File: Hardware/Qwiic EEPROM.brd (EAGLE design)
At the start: 25.4 x 25.4 mm, 56 parts, among them J3 PTH, U1 RM24C512C

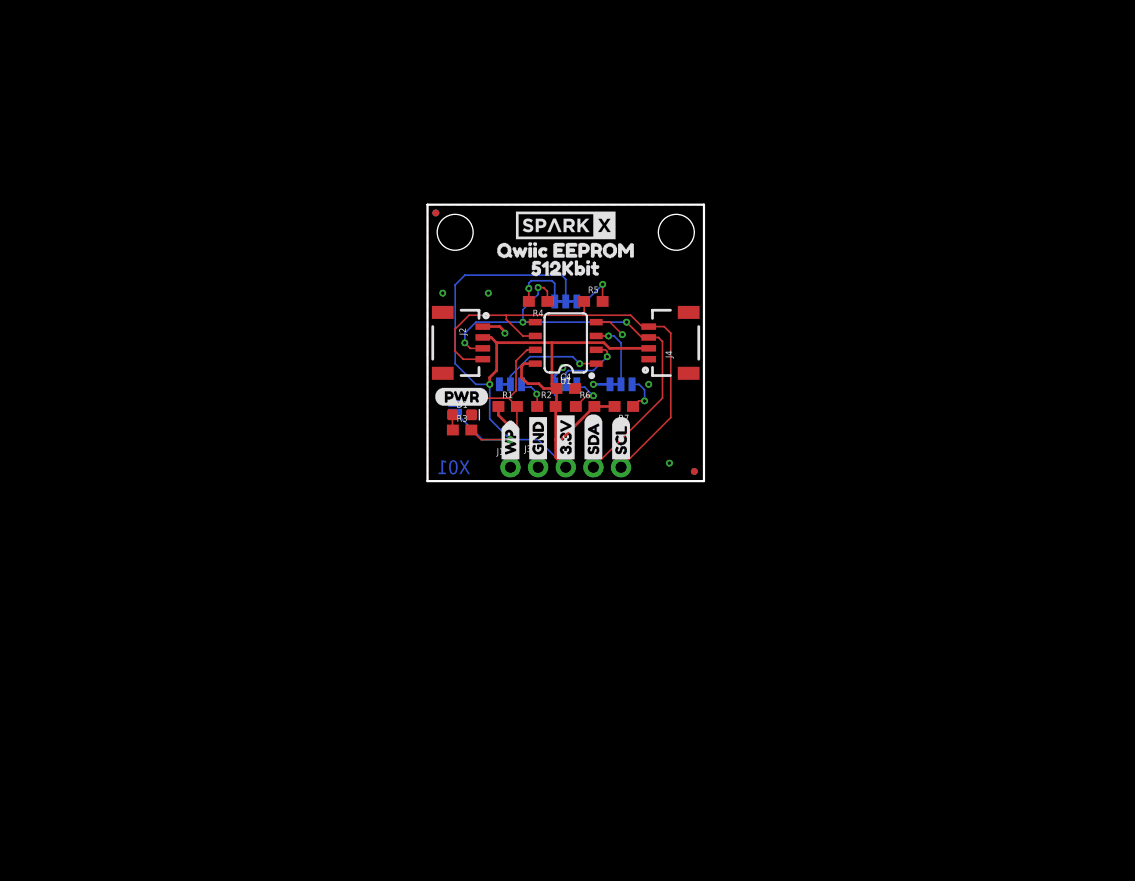
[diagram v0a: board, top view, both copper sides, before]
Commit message: Add datasheet, make sure all parts are from SF libraries
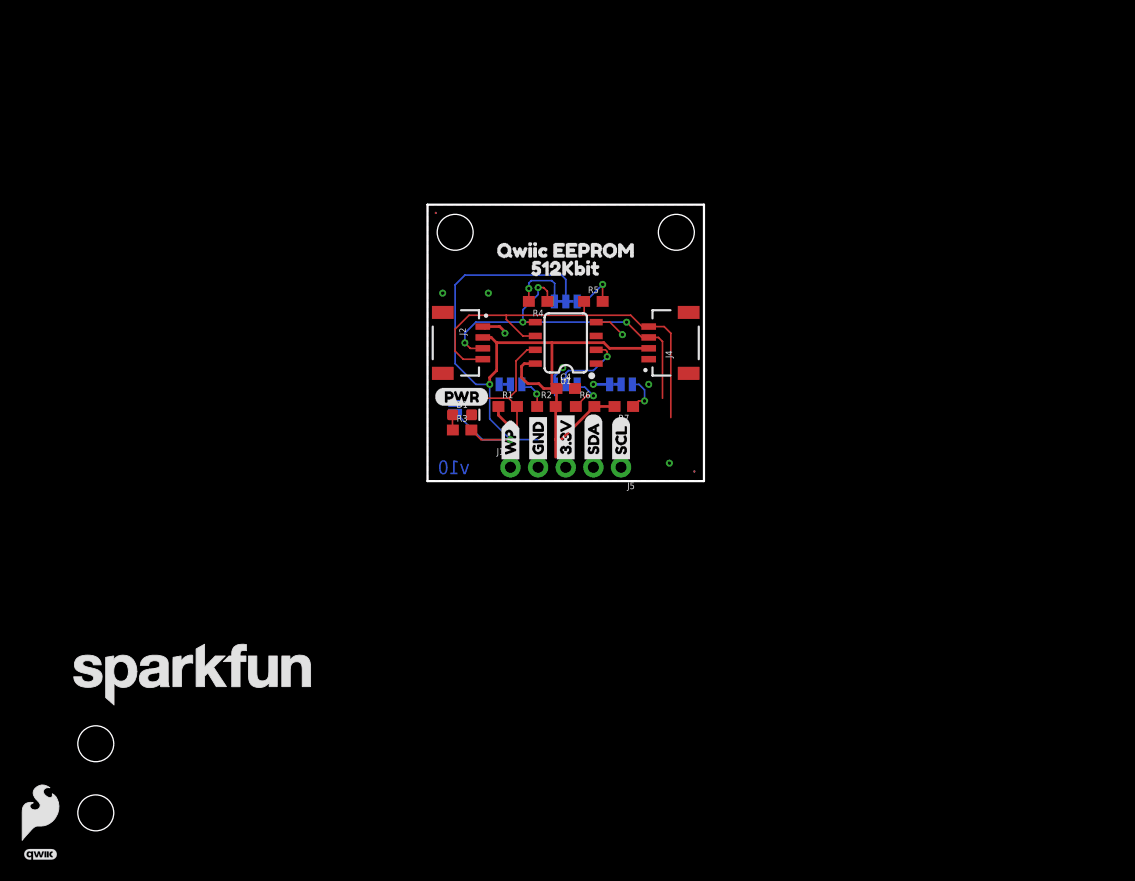
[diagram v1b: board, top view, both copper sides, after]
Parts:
- removed J3: PTH, SparkX:1X04_NO_SILK
- removed U$1, U$2: SPARKX-LOGO4, SparkX:SPARKX-MEDIUM
- added J5: (no value), SparkFun-Connectors:1X04_NO_SILK
- added JP7, JP8: STAND-OFF, SparkFun-Hardware:STAND-OFF
- added LOGO2: SFE_LOGO_NAME.2_INCH, SparkFun-Aesthetics:SFE_LOGO_NAME_.2
- added LOGO3: SFE_LOGO_FLAME.2_INCH, SparkFun-Aesthetics:SFE_LOGO_FLAME_.2
- added LOGO4: QWIIC_LOGO_3MM, SparkFun-Aesthetics:QWIIC_3MM
- E0, E1, E2: value (none) -> JUMPER-SMT_3_1-NC_TRACE_SILK
- I2C: value (none) -> JUMPER-SMT_3_2-NC_TRACE_SILK
- J2, J4: value (none) -> QWIIC_RA; device SparkFun-Connectors:1X04_1MM_RA -> SparkFun-Connectors:JST04_1MM_RA
- JP1, JP2, JP5, JP6: value FIDUCIALUFIDUCIAL -> FIDUCIAL0.2MM; device SparkFun:MICRO-FIDUCIAL -> SparkFun-Aesthetics:FIDUCIAL-0.2MM
- JP3, JP4: device SparkFun:STAND-OFF -> SparkFun-Hardware:STAND-OFF
- R4, R5: value 2.2k -> 4.7k
- WP: value (none) -> JUMPER-SMT_2_NO_SILK
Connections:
- net 3.3V: now also J5.3; no longer J3.2
- net GND: now also J5.4; no longer J3.1
- net SCL: now also J5.1; no longer J3.4
- net SDA: now also J5.2; no longer J3.3
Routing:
- net N$6: track 9.81 -> 0.00 mm, vias 1 -> 0
- net SDA: track 43.1 -> 34.1 mm
- net SCL: track 45.1 -> 38.6 mm
- net N$4: track 6.35 -> 0.00 mm, vias 1 -> 0
- net 3.3V: track 93.4 -> 87.3 mm
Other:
- board text added: "Revised by: Priyanka Makin"
- board text added: "v10"
- board text removed: "X01"

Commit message: Hardware updates
Schematic symbols from current SF libs
Added mounting holes
re-routing
Update 3.3V rail width
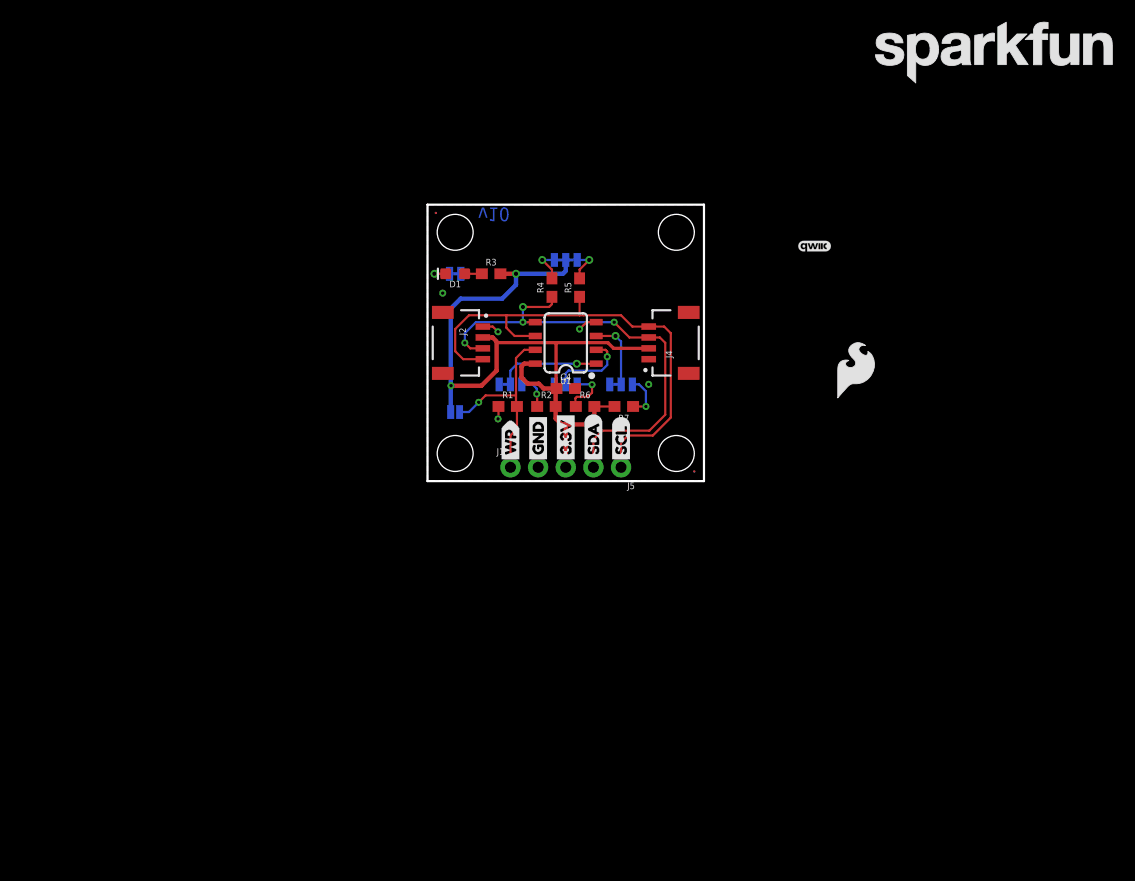
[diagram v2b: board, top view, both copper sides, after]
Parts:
- removed U$10: (no value), Labels-0_04:(PWR)
- removed U$14, U$17: (no value), buzzard_labels:512KBIT7
- removed U$15, U$16: (no value), buzzard_labels:QWIIC_EEPROM2
- removed U$29: (no value), Labels:QWIIC-LOGO-MEDIUM
- added POWER: JUMPER-SMT_2_NC_TRACE_SILK, SparkFun-Jumpers:SMT-JUMPER_2_NC_TRACE_SILK
- moved LOGO2 93.2 mm to (52.1, 39.4)
- moved LOGO4 90.4 mm to (35.6, 21.6)
- moved LOGO3 85.2 mm to (39.4, 10.2)
- moved JP8 62.7 mm to (22.9, 2.54)
- moved JP7 42.4 mm to (2.54, 2.54)
- moved LOGO1 28.5 mm to (29.2, 14.0)
- moved R3 14.6 mm to (5.84, 19.1)
- moved D1 13.0 mm to (2.54, 19.1), turned to 180 degrees
- moved I2C 3.81 mm to (12.7, 20.3)
- moved R4 1.80 mm to (11.4, 17.8), turned to 90 degrees
- moved R5 1.80 mm to (14.0, 17.8), turned to 90 degrees
- moved WP 0.38 mm to (2.54, 6.35), turned to 0 degrees
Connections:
- new net N$10: D1.C, POWER.2
- net GND: now also POWER.1; no longer D1.C
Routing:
- net 3.3V: track 87.3 -> 71.6 mm
- net SDA: track 34.1 -> 45.0 mm
- net N$6: track 0.00 -> 9.42 mm, vias 0 -> 1
- net SCL: track 38.6 -> 47.3 mm
- net GND: track 12.1 -> 4.55 mm, vias 9 -> 5
- net N$4: track 0.00 -> 6.43 mm, vias 0 -> 1
- net N$2: track 5.91 -> 3.18 mm
- net N$10: track 0.00 -> 2.41 mm, vias 0 -> 1
- net N$1: track 4.56 -> 3.18 mm

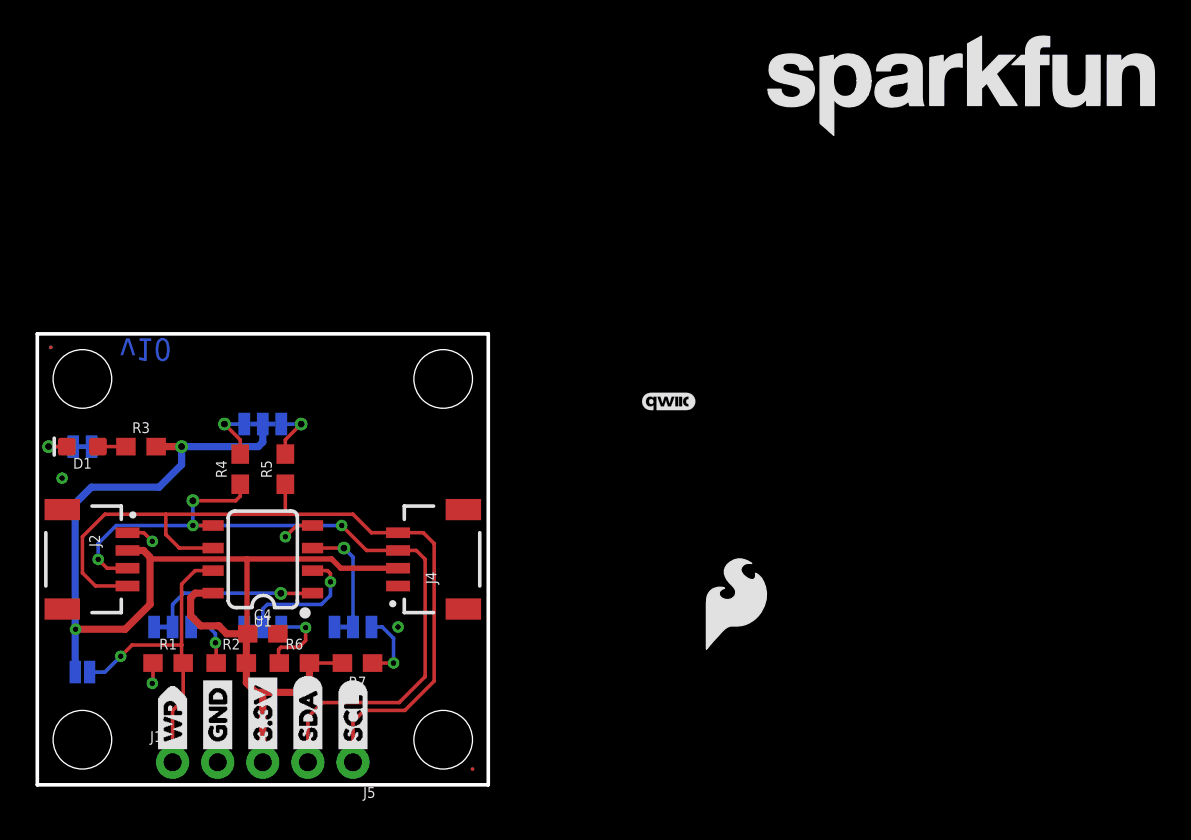
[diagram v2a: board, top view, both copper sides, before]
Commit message: Vectorize labels
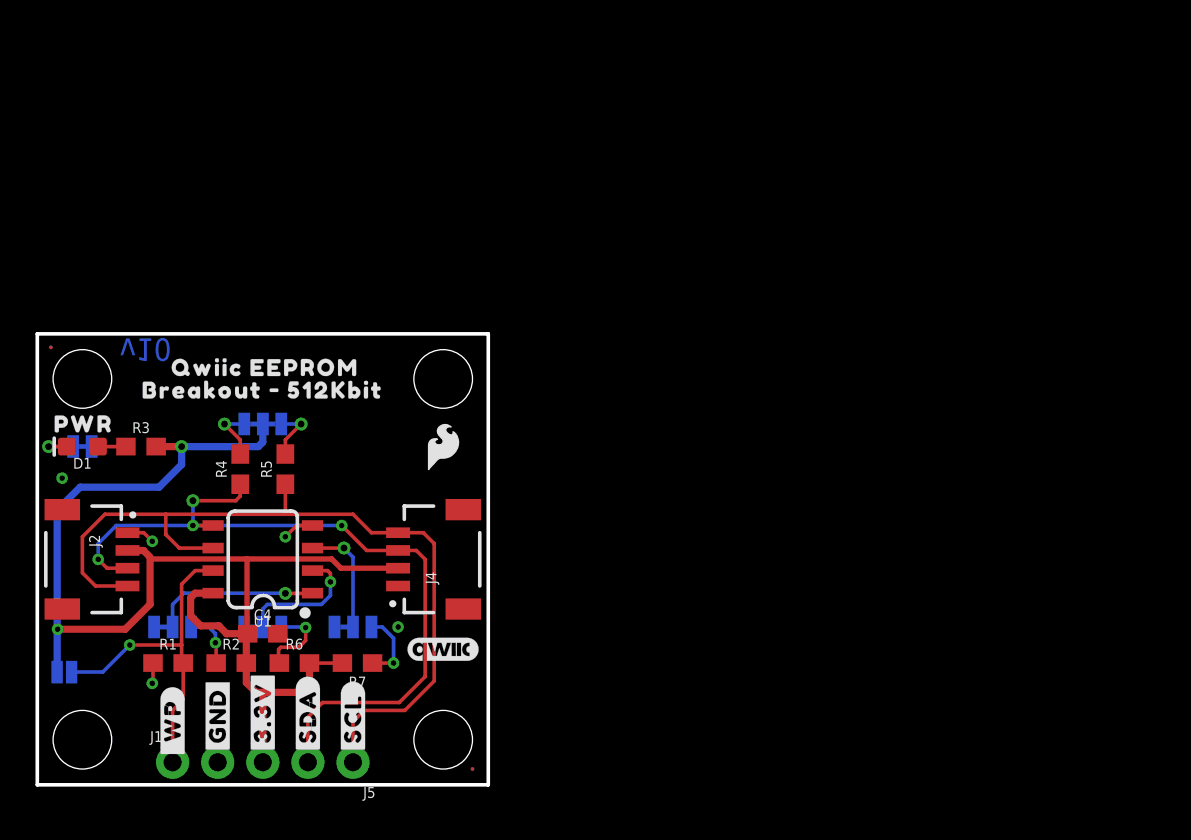
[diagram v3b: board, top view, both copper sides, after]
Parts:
- removed U$25, U$28: (no value), buzzard_labels (2):WP2
- removed U$26: (no value), Labels-0_04:SCL9
- removed U$27: (no value), Labels-0_04:SDA8
- added U$1, U$2: (no value), output:#_WP#0
- added U$10, U$14: (no value), output:#GND#0
- added U$15, U$16: (no value), output:#3#3V#0
- added U$17, U$29: (no value), output:#SDA#0
- added U$30, U$31: (no value), output:#SCL#0
- LOGO2: value SFE_LOGO_NAME.2_INCH -> SFE_LOGO_NAME.1_INCH; device SparkFun-Aesthetics:SFE_LOGO_NAME_.2 -> SparkFun-Aesthetics:SFE_LOGO_NAME_.1
- LOGO3: value SFE_LOGO_FLAME.2_INCH -> SFE_LOGO_FLAME.1_INCH; device SparkFun-Aesthetics:SFE_LOGO_FLAME_.2 -> SparkFun-Aesthetics:SFE_LOGO_FLAME_.1
- LOGO4: value QWIIC_LOGO_3MM -> QWIIC_LOGO_4MM; device SparkFun-Aesthetics:QWIIC_3MM -> SparkFun-Aesthetics:QWIIC_4MM
- U$12: device buzzard_labels (1):00 -> output:PWR0
- U$13: device buzzard_labels:E14 -> output:10
- U$18: device buzzard_labels (1):00 -> output:#PWR#0
- U$19: device buzzard_labels (1):00 -> output:QWIIC_EEPROM0
- U$20: device buzzard_labels (1):11 -> output:QWIIC_EEPROM0
- U$21: device Labels-0_04:3#3V2 -> output:10
- U$22: device Labels-0_04:GND1 -> output:10
- U$23, U$24: device buzzard_labels (1):11 -> output:BREAKOUT_#_512KBIT0
- U$3: device Labels-0_04:GND1 -> output:#WP#0
- U$4: device Labels-0_04:3#3V2 -> output:E00
- U$5: device Labels-0_04:SDA8 -> output:E10
- U$6: device Labels-0_04:SCL9 -> output:E20
- U$7: device buzzard_labels:WP6 -> output:00
- U$8: device buzzard_labels:E05 -> output:00
- U$9: device buzzard_labels:E23 -> output:00
- moved LOGO2 46.9 mm to (12.7, 14.0), flipped to the bottom
- moved U$12 22.5 mm to (0.25, 20.3), flipped to the top
- moved LOGO4 18.9 mm to (22.9, 7.62)
- moved LOGO3 18.8 mm to (22.9, 19.1)
- moved U$23 18.3 mm to (5.21, 22.2), flipped to the top
- moved U$24 18.1 mm to (20.1, 22.2)
- moved U$20 16.6 mm to (18.7, 23.5)
- moved U$19 16.6 mm to (6.86, 23.5), flipped to the top
- moved U$18 13.0 mm to (8.13, 18.9)
- moved LOGO1 9.92 mm to (22.9, 6.35)
- moved U$4 9.81 mm to (9.14, 10.7), turned to 0 degrees
- moved U$6 9.27 mm to (19.3, 10.7), turned to 0 degrees
- moved U$5 9.20 mm to (14.2, 10.7), turned to 0 degrees
- moved U$13 6.43 mm to (19.8, 6.99)
- moved U$3 6.31 mm to (6.10, 6.35), turned to 0 degrees
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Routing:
- net 3.3V: track 71.6 -> 73.4 mm
- net WP: track 18.2 -> 19.2 mm

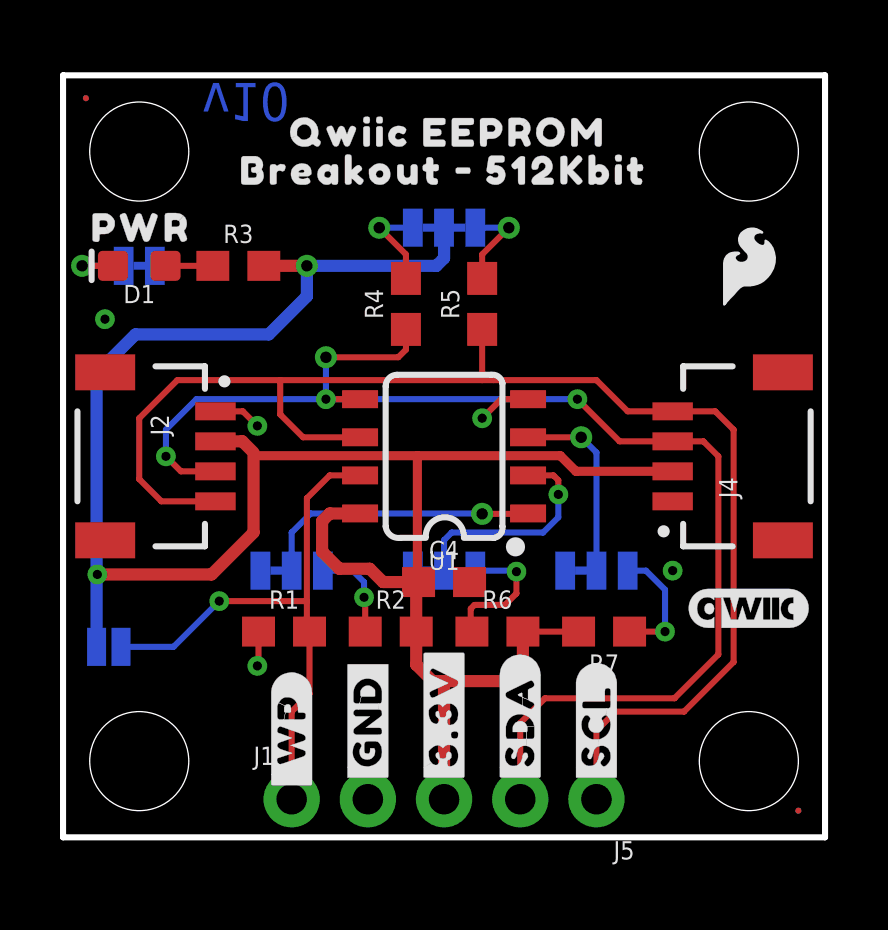
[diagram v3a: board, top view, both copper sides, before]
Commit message: Design review changes
Schematic:
* Added Vcc range for EEPROM IC
* Updated notes for power led and address jumpers
* Got rid of legacy font
* Replaced pullup/pulldown resistors R1, R2, R6, R7 to 100k

Board:
* Weird tRestrict on GND pad of EEPROM IC --> moved via around to avoid DRC errors
* Moved "PWR" label underneath the LED
* Moved "I2C" label so that it touches the silk of the jumper above it
* Re-routed 3.3V trace so that it does not run under the EEPROM IC
* Increased size of fiducials
* Made vias all the same size
* Added prod-id to the EEPROM IC
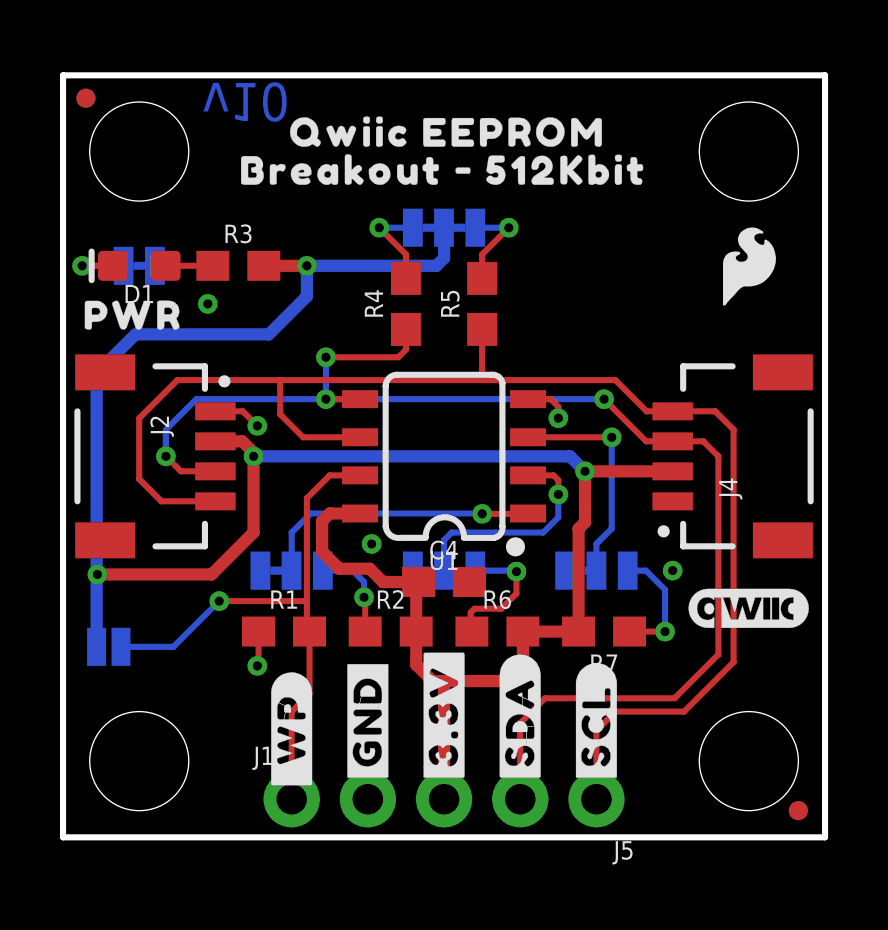
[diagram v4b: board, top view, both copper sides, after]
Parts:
- JP1, JP2, JP5, JP6: value FIDUCIAL0.2MM -> FIDUCIALUFIDUCIAL; device SparkFun-Aesthetics:FIDUCIAL-0.2MM -> SparkFun-Aesthetics:FIDUCIAL-MICRO
- R1, R2, R6, R7: value 10k -> 100k
- moved U$12 2.93 mm to (0.00, 17.4)
- moved U$11 0.38 mm to (14.6, 18.5)
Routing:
- net 3.3V: track 73.4 -> 74.6 mm, vias 2 -> 4
- net N$4: track 6.43 -> 7.44 mm
- net GND: track 4.55 -> 4.25 mm, vias 5 -> 6
